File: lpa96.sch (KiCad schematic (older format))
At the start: 26 parts, among them IC1 ATMEGA328-A, P1 CONN_2, P2 CONN_3X2, SW1 SW_PUSH, U1 SD_CARD, U2 LD1117S33, Y1 RESONATEUR

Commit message: updated 3d models & footprint references
changed P1 and P2 library part models to match part from BOM
added Molex step model for P1
fixed U2 SOT223 model to use modern STEP model instead of old .wrl
updated resistor/capacitor footprints to match KiCAD5 library name changes
deleted fp-info-cache and added to git ignore (not needed, generated dynamically)
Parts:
- C1, C2: footprint Capacitors_SMD:C_0805 -> Capacitor_SMD:C_0805_2012Metric
- C5: footprint Capacitors_SMD:C_1206 -> Capacitor_SMD:C_1206_3216Metric
- LED97, LED98, LED99: footprint LEDs:LED_0805 -> LED_SMD:LED_0805_2012Metric
- R1, R10, R11, R15, R16, R17, R18, R19, R2, R9: footprint Resistors_SMD:R_0805 -> Resistor_SMD:R_0805_2012Metric
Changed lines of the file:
@@
 F 0 "R11" V 4130 6800 40  0000 C CNN
 F 1 "330" V 3950 6800 40  0000 C CNN
-F 2 "Resistors_SMD:R_0805" V 3980 6800 30  0001 C CNN
+F 2 "Resistor_SMD:R_0805_2012Metric" V 3980 6800 30  0001 C CNN
 F 3 "~" H 4050 6800 30  0000 C CNN
 F 4 "5% Chip Resistor 0805" H 4050 6800 50  0001 C CNN "Description"
@@
 F 0 "R10" V 4130 6500 40  0000 C CNN
 F 1 "330" V 3950 6500 40  0000 C CNN
-F 2 "Resistors_SMD:R_0805" V 3980 6500 30  0001 C CNN
+F 2 "Resistor_SMD:R_0805_2012Metric" V 3980 6500 30  0001 C CNN
 F 3 "~" H 4050 6500 30  0000 C CNN
 F 4 "5% Chip Resistor 0805" H 4050 6500 50  0001 C CNN "Description"
@@
 F 0 "R9" V 4130 6200 40  0000 C CNN
 F 1 "330" V 3950 6200 40  0000 C CNN
-F 2 "Resistors_SMD:R_0805" V 3980 6200 30  0001 C CNN
+F 2 "Resistor_SMD:R_0805_2012Metric" V 3980 6200 30  0001 C CNN
 F 3 "~" H 4050 6200 30  0000 C CNN
 F 4 "5% Chip Resistor 0805" H 4050 6200 50  0001 C CNN "Description"
@@
 F 0 "C2" H 6400 4050 40  0000 L CNN
 F 1 "100nF" H 6300 4250 40  0000 L CNN
-F 2 "Capacitors_SMD:C_0805" H 6538 4000 30  0001 C CNN
+F 2 "Capacitor_SMD:C_0805_2012Metric" H 6538 4000 30  0001 C CNN
 F 3 "~" H 6500 4150 60  0000 C CNN
 F 4 "-20/+80% 50V Y5V SMD MLCC Capacitor 0805" H 6500 4150 50  0001 C CNN "Description"
@@
 F 0 "C1" H 6550 3850 40  0000 L CNN
 F 1 "100nF" H 6550 4050 40  0000 L CNN
-F 2 "Capacitors_SMD:C_0805" H 6538 3800 30  0001 C CNN
+F 2 "Capacitor_SMD:C_0805_2012Metric" H 6538 3800 30  0001 C CNN
 F 3 "~" H 6500 3950 60  0000 C CNN
 F 4 "-20/+80% 50V Y5V SMD MLCC Capacitor 0805" H 6500 3950 50  0001 C CNN "Description"
@@
 F 0 "R1" V 4480 7650 40  0000 C CNN
 F 1 "10k" V 4300 7650 40  0000 C CNN
-F 2 "Resistors_SMD:R_0805" V 4330 7650 30  0001 C CNN
+F 2 "Resistor_SMD:R_0805_2012Metric" V 4330 7650 30  0001 C CNN
 F 3 "~" H 4400 7650 30  0000 C CNN
 F 4 "5% Chip Resistor 0805" H 4400 7650 50  0001 C CNN "Description"
@@
 F 0 "R2" V 6380 1750 40  0000 C CNN
 F 1 "10k" V 6307 1751 40  0000 C CNN
-F 2 "Resistors_SMD:R_0805" V 6230 1750 30  0001 C CNN
+F 2 "Resistor_SMD:R_0805_2012Metric" V 6230 1750 30  0001 C CNN
 F 3 "~" H 6300 1750 30  0000 C CNN
 F 4 "5% Chip Resistor 0805" H 6300 1750 50  0001 C CNN "Description"
@@
 F 0 "R15" V 3230 1250 40  0000 C CNN
 F 1 "47k" V 3150 1250 40  0000 C CNN
-F 2 "Resistors_SMD:R_0805" V 3080 1250 30  0001 C CNN
+F 2 "Resistor_SMD:R_0805_2012Metric" V 3080 1250 30  0001 C CNN
 F 3 "~" H 3150 1250 30  0000 C CNN
 F 4 "5% Chip Resistor 0805" H 3150 1250 50  0001 C CNN "Description"
@@
 F 0 "R16" V 3430 1250 40  0000 C CNN
 F 1 "47k" V 3357 1251 40  0000 C CNN
-F 2 "Resistors_SMD:R_0805" V 3280 1250 30  0001 C CNN
+F 2 "Resistor_SMD:R_0805_2012Metric" V 3280 1250 30  0001 C CNN
 F 3 "~" H 3350 1250 30  0000 C CNN
 F 4 "5% Chip Resistor 0805" H 3350 1250 50  0001 C CNN "Description"
@@
 F 0 "R17" V 3630 1250 40  0000 C CNN
 F 1 "47k" V 3557 1251 40  0000 C CNN
-F 2 "Resistors_SMD:R_0805" V 3480 1250 30  0001 C CNN
+F 2 "Resistor_SMD:R_0805_2012Metric" V 3480 1250 30  0001 C CNN
 F 3 "~" H 3550 1250 30  0000 C CNN
 F 4 "5% Chip Resistor 0805" H 3550 1250 50  0001 C CNN "Description"
@@
 F 0 "R18" V 3830 1250 40  0000 C CNN
 F 1 "47k" V 3757 1251 40  0000 C CNN
-F 2 "Resistors_SMD:R_0805" V 3680 1250 30  0001 C CNN
+F 2 "Resistor_SMD:R_0805_2012Metric" V 3680 1250 30  0001 C CNN
 F 3 "~" H 3750 1250 30  0000 C CNN
 F 4 "5% Chip Resistor 0805" H 3750 1250 50  0001 C CNN "Description"
@@
 F 0 "R19" V 4030 1250 40  0000 C CNN
 F 1 "47k" V 3957 1251 40  0000 C CNN
-F 2 "Resistors_SMD:R_0805" V 3880 1250 30  0001 C CNN
+F 2 "Resistor_SMD:R_0805_2012Metric" V 3880 1250 30  0001 C CNN
 F 3 "~" H 3950 1250 30  0000 C CNN
 F 4 "5% Chip Resistor 0805" H 3950 1250 50  0001 C CNN "Description"
@@
 F 0 "LED97" H 4600 6100 50  0000 C CNN
 F 1 "LED_ALT" H 4593 6036 50  0001 C CNN
-F 2 "LEDs:LED_0805" H 4600 6200 50  0001 C CNN
+F 2 "LED_SMD:LED_0805_2012Metric" H 4600 6200 50  0001 C CNN
 F 3 "~" H 4600 6200 50  0001 C CNN
 F 4 "SMD LED Green 0805" H 4600 6200 50  0001 C CNN "Description"
@@
 F 0 "LED98" H 4600 6400 50  0000 C CNN
 F 1 "LED_ALT" H 4593 6336 50  0001 C CNN
-F 2 "LEDs:LED_0805" H 4600 6500 50  0001 C CNN
+F 2 "LED_SMD:LED_0805_2012Metric" H 4600 6500 50  0001 C CNN
 F 3 "~" H 4600 6500 50  0001 C CNN
 F 4 "SMD LED Red 0805" H 4600 6500 50  0001 C CNN "Description"
@@
 F 0 "LED99" H 4600 6700 50  0000 C CNN
 F 1 "LED_ALT" H 4593 6636 50  0001 C CNN
-F 2 "LEDs:LED_0805" H 4600 6800 50  0001 C CNN
+F 2 "LED_SMD:LED_0805_2012Metric" H 4600 6800 50  0001 C CNN
 F 3 "~" H 4600 6800 50  0001 C CNN
 F 4 "SMD LED Yellow 0805" H 4600 6800 50  0001 C CNN "Description"
@@
 F 0 "C5" H 3950 4600 40  0000 L CNN
 F 1 "10uF" H 3956 4415 40  0000 L CNN
-F 2 "Capacitors_SMD:C_1206" H 3988 4350 30  0001 C CNN
+F 2 "Capacitor_SMD:C_1206_3216Metric" H 3988 4350 30  0001 C CNN
 F 3 "~" H 3950 4500 60  0000 C CNN
 F 4 "10% 25V X5R SMD MLCC Capacitor 1206" H 3950 4500 50  0001 C CNN "Description"

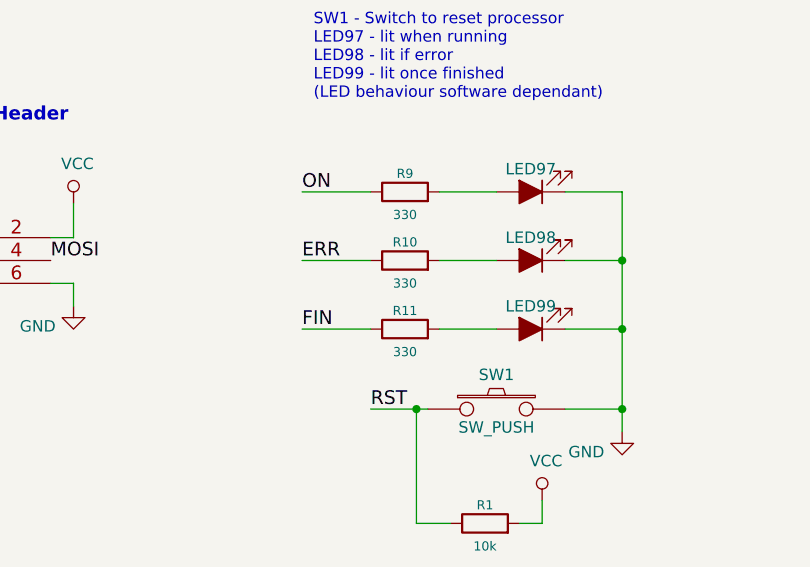
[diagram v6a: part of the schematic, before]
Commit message: changed '330" resistor value to "330R"
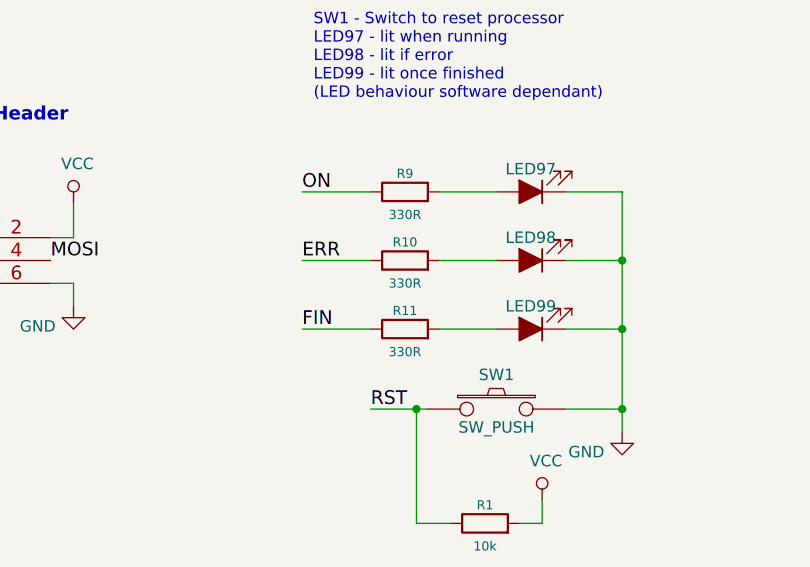
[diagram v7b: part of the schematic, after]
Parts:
- R10, R11, R9: value 330 -> 330R
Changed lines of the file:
@@
 P 4050 6800
 F 0 "R11" V 4130 6800 40  0000 C CNN
-F 1 "330" V 3950 6800 40  0000 C CNN
+F 1 "330R" V 3950 6800 40  0000 C CNN
 F 2 "Resistor_SMD:R_0805_2012Metric" V 3980 6800 30  0001 C CNN
 F 3 "~" H 4050 6800 30  0000 C CNN
@@
 P 4050 6500
 F 0 "R10" V 4130 6500 40  0000 C CNN
-F 1 "330" V 3950 6500 40  0000 C CNN
+F 1 "330R" V 3950 6500 40  0000 C CNN
 F 2 "Resistor_SMD:R_0805_2012Metric" V 3980 6500 30  0001 C CNN
 F 3 "~" H 4050 6500 30  0000 C CNN
@@
 P 4050 6200
 F 0 "R9" V 4130 6200 40  0000 C CNN
-F 1 "330" V 3950 6200 40  0000 C CNN
+F 1 "330R" V 3950 6200 40  0000 C CNN
 F 2 "Resistor_SMD:R_0805_2012Metric" V 3980 6200 30  0001 C CNN
 F 3 "~" H 4050 6200 30  0000 C CNN
